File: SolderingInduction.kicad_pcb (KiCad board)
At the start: 4 copper layers, 68.9 x 37.6 mm, 52 parts, among them J1 MC-307, J3 RBP_GPIO_CONN, SW1 SW_Push, SW2 SW_Push, SW3 SW_Push, SW4 SW_Push, SW5 SW_Push, SW6 SW_Push, SW7 SW_Push, SW8 SW_Push, U1 SPX2920M3-3.3_SOT223, U3 W25Q32JVZP, U4 RP2040, Y1 X322512MMB4SI

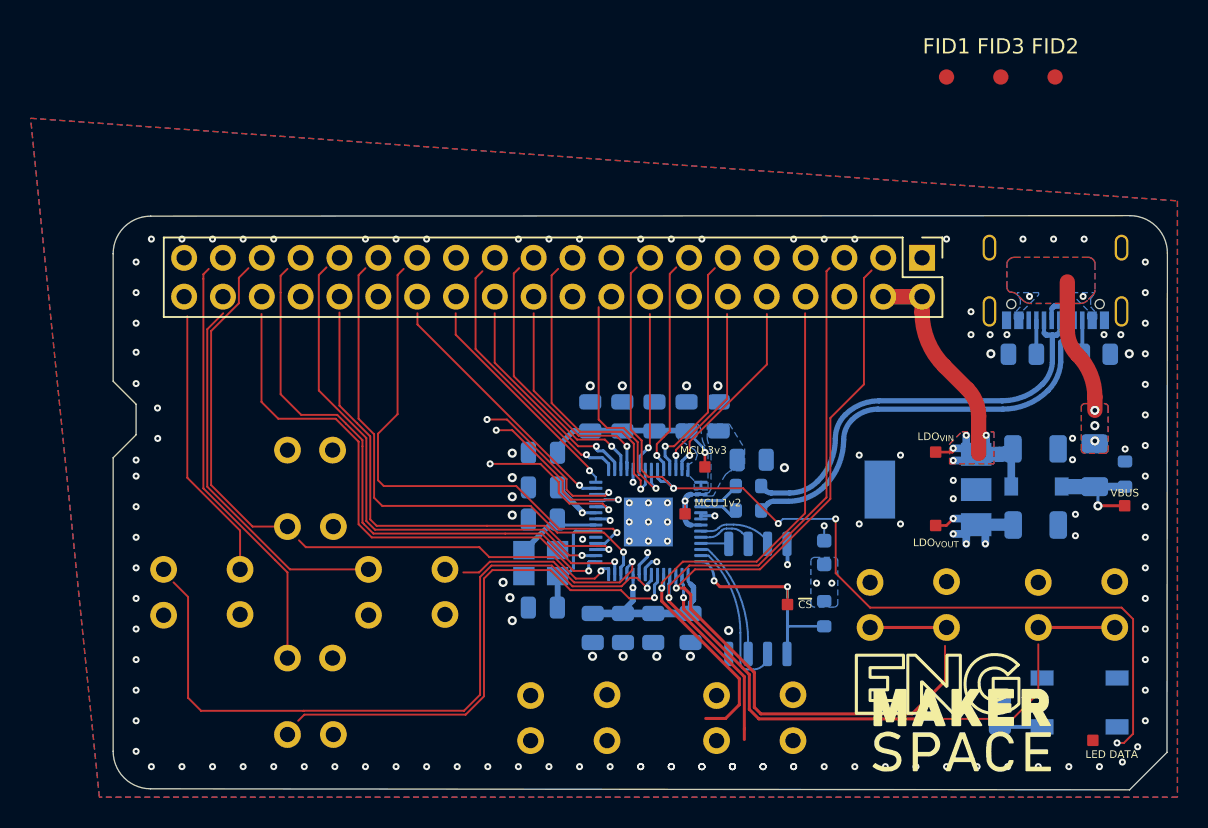
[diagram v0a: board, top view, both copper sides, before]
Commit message: SWD pad breakout
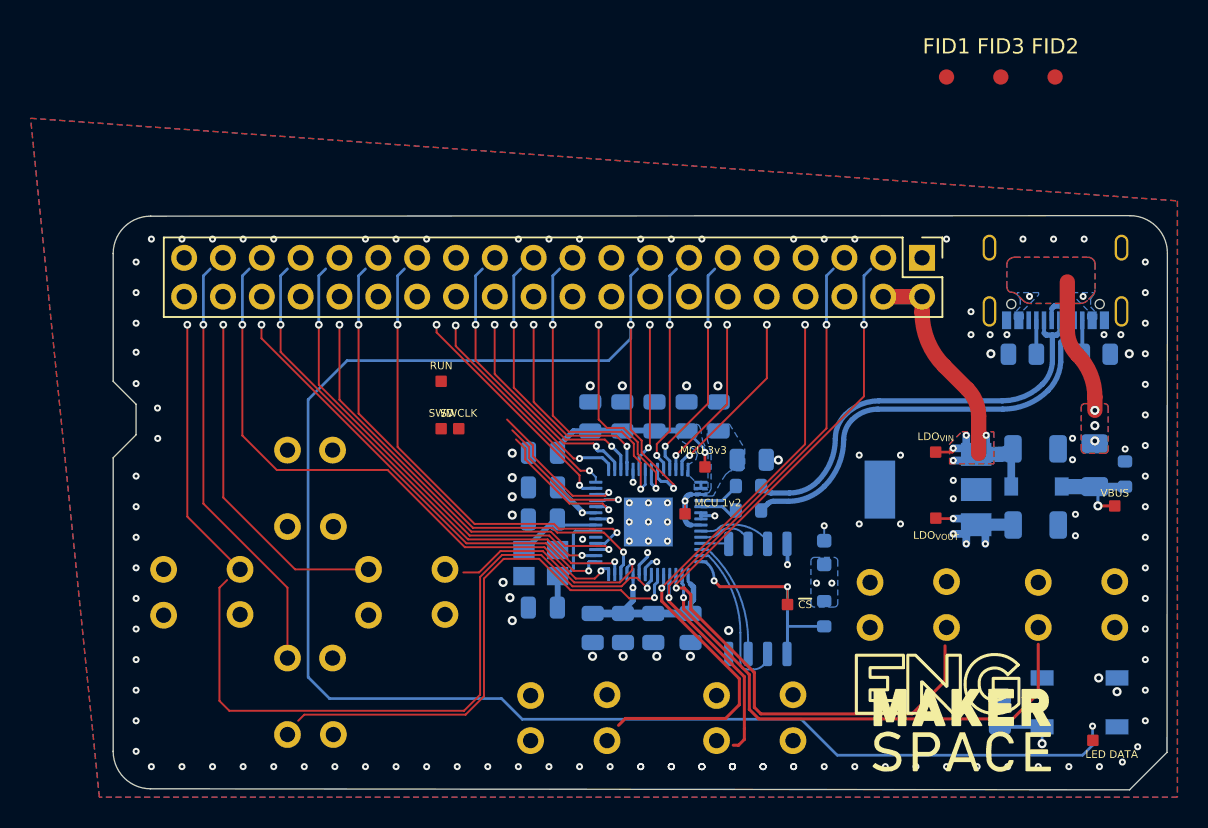
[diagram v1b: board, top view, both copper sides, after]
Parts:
- added TP3: RUN, 0:Testpoint_Custom, F.Cu at (111.5, 65.8)
- added TP4: SWCLK, 0:Testpoint_Custom, F.Cu at (112.6, 68.9)
- added TP6: SWD, 0:Testpoint_Custom, F.Cu at (111.5, 68.9)
- moved TP8 0.65 mm to (155.5, 74.0)
- moved TP9 0.48 mm to (143.8, 74.8)
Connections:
- U4 pad 24: unconnected-(U4-Pad24) -> Net-(U4-Pad24)
- U4 pad 25: unconnected-(U4-Pad25) -> Net-(U4-Pad25)
- U4 pad 26: unconnected-(U4-Pad26) -> Net-(U4-Pad26)
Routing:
- net /$.GPIO25: track 62.9 -> 114.3 mm, vias 4 -> 3
- net /BUTTON_SELECT: track 21.3 -> 0.00 mm
- net /$.GPIO11: track 22.0 -> 39.6 mm, vias 1 -> 2
- net unconnected-(U4-Pad25): track 11.8 -> 0.00 mm, vias 2 -> 0
- net unconnected-(U4-Pad26): track 11.4 -> 0.00 mm, vias 2 -> 0
- net Net-(U4-Pad25): track 0.00 -> 10.7 mm, vias 0 -> 1
- net unconnected-(U4-Pad24): track 10.3 -> 0.00 mm, vias 2 -> 0
- net Net-(U4-Pad26): track 0.00 -> 10.1 mm, vias 0 -> 1
- net Net-(U4-Pad24): track 0.00 -> 9.31 mm, vias 0 -> 1
- net /$.GPIO12: track 35.9 -> 29.6 mm, vias 1 -> 2
- net /BUTTON_START: track 5.00 -> 0.00 mm
- net /BUTTON_RIGHT: track 5.00 -> 0.00 mm
- net /$.GPIO10: track 38.9 -> 34.1 mm, vias 1 -> 2
- net /$.GPIO14: track 31.6 -> 27.4 mm, vias 1 -> 2
- net /$.GPIO13: track 34.0 -> 30.5 mm, vias 1 -> 2
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
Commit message: Fiducials, Testpoints, routing cleanup
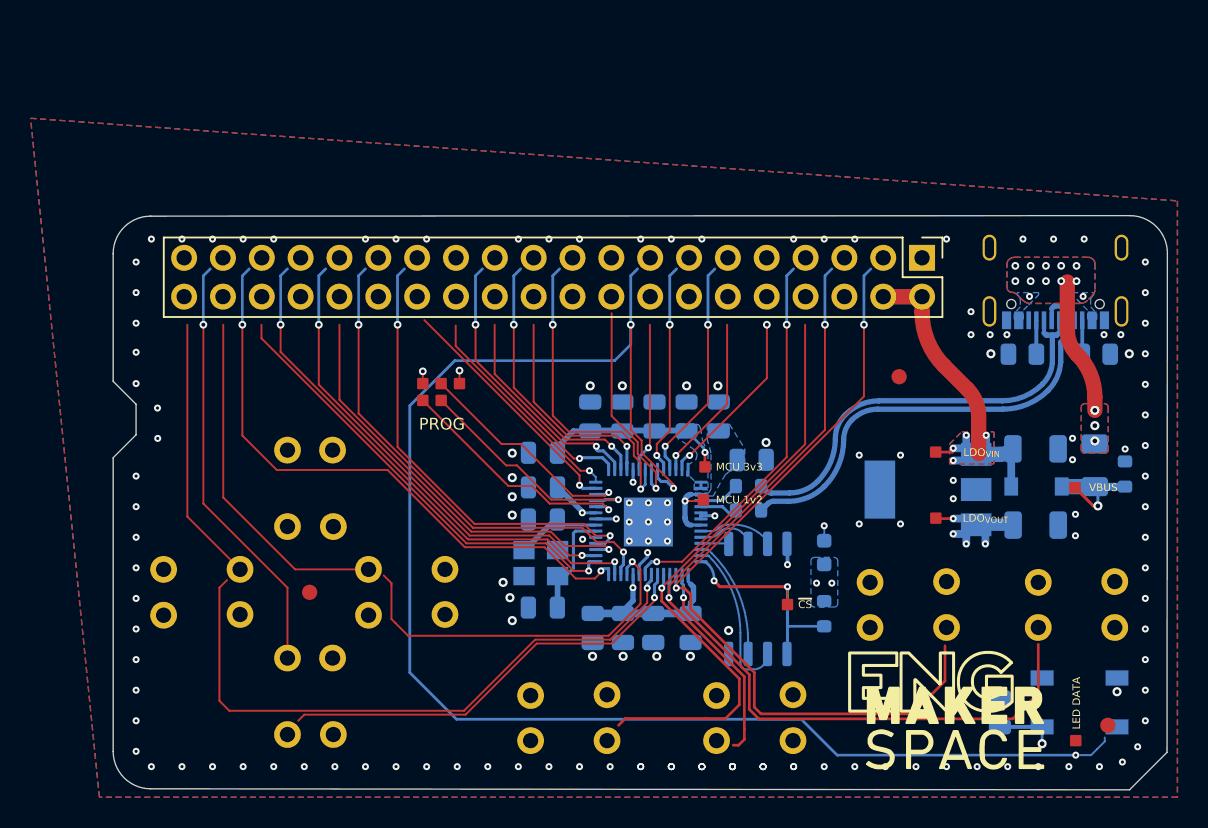
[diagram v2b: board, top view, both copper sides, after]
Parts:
- added TP11: SWD_3V3, 0:Testpoint_Custom, F.Cu at (112.7, 66.0)
- added TP7: RUN_GND, 0:Testpoint_Custom, F.Cu at (110.2, 66.0)
- moved FID1 53.6 mm to (102.8, 79.6)
- moved FID2 42.5 mm to (155.1, 88.3)
- moved FID3 20.7 mm to (141.4, 65.5)
- moved TP4 2.99 mm to (110.2, 67.0)
- moved TP8 2.86 mm to (152.9, 72.8)
- moved TP6 1.85 mm to (111.5, 67.0)
- moved TP2 1.51 mm to (128.6, 73.5)
- moved TP5 1.12 mm to (152.9, 89.3)
- moved REF** 0.46 mm to (138.2, 83.6)
- moved TP3 0.15 mm to (111.5, 66.0)
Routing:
- net /$.GPIO6: track 1.35 -> 25.2 mm, vias 1 -> 2
- net /$.GPIO25: track 114.3 -> 100.7 mm
- net /$.GPIO8: track 14.2 -> 24.5 mm
- net Net-(U4-Pad24): track 9.31 -> 16.1 mm
- net /$.GPIO4: track 34.9 -> 28.4 mm
- net /$.GPIO5: track 47.4 -> 41.2 mm
- net Net-(U4-Pad25): track 10.7 -> 15.8 mm
- net Net-(U4-Pad26): track 10.1 -> 15.0 mm
- net +3V3: track 50.0 -> 51.2 mm, vias 13 -> 14
- net VBUS: track 10.4 -> 11.3 mm
- net /$.GPIO15: track 30.2 -> 29.4 mm
- net GND: track 1.15 -> 1.95 mm
- net /$.GPIO16: track 15.5 -> 16.1 mm, vias 2 -> 1
- net /$.GPIO24: track 14.2 -> 14.0 mm, vias 2 -> 1
- net /USB_VBUS: vias 5 -> 15
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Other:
- board text added: "PROG"

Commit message: Testpoint grid alignment + spacing
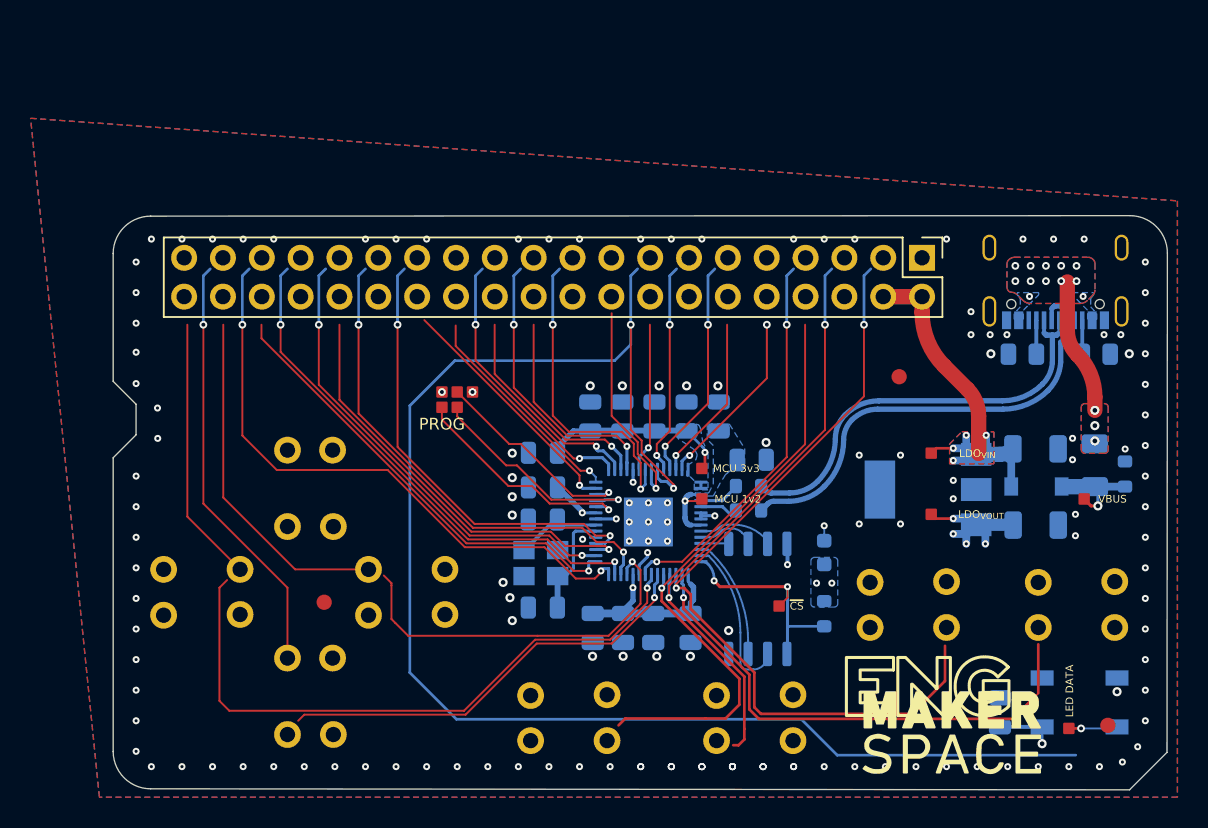
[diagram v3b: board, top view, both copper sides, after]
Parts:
- moved TP7 1.37 mm to (111.5, 66.5)
- moved TP4 1.33 mm to (111.5, 67.5)
- moved TP3 1.19 mm to (112.5, 66.5)
- moved FID1 1.15 mm to (103.8, 80.2)
- moved TP6 1.14 mm to (112.5, 67.5)
- moved TP11 1.01 mm to (113.5, 66.5)
- moved TP8 0.96 mm to (153.5, 73.5)
- moved TP5 0.92 mm to (152.5, 88.5)
- moved TP12 0.56 mm to (133.6, 80.5)
- moved TP9 0.39 mm to (143.5, 74.5)
- moved REF** 0.36 mm to (137.9, 83.8)
- moved TP10 0.30 mm to (143.5, 70.5)
- moved TP1 0.22 mm to (128.5, 71.5)
- moved TP2 0.11 mm to (128.5, 73.5)
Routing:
- net /LED_{DI}: track 0.00 -> 3.19 mm, vias 0 -> 1
- net /$.GPIO25: track 100.7 -> 98.2 mm, vias 3 -> 2
- net Net-(U4-Pad26): track 15.0 -> 13.7 mm
- net Net-(U4-Pad24): track 16.1 -> 15.1 mm
- net VBUS: track 11.3 -> 10.4 mm
- net Net-(U4-Pad25): track 15.8 -> 14.9 mm
- net GND: track 1.95 -> 1.15 mm, vias 149 -> 150
